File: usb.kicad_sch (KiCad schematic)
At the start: 23 parts, among them IC2 USB Hub, J2 2-Port USB, J3 2-Port USB

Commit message: USB stack changes
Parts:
- added C30, C31: 27pF, Capacitor_SMD:C_0805_2012Metric, symbol group127:0805Capacitor
- added J8: USB_Headers, Connector_PinHeader_2.54mm:PinHeader_1x04_P2.54mm_Vertical, symbol Connector:Conn_01x04_Pin
- added R31: 1.5kOhm, Resistor_SMD:R_0805_2012Metric, symbol group127:Resistor
- added Y1: ECS-060-20-4X-DU, group127:XTAL_ECS-160-20-4X, symbol group127:ECS-060-20-4X-DU
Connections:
- net TSTPLL/48MCLK is gone; now on net GND: IC2.27 (TSTPLL/48MCLK)
- net 3V3: no longer IC2.30 (XTAL1), IC2.31 (TSTMODE)
- net 5V: now also J8.1 (Pin_1)
- net GND: now also IC2.31 (TSTMODE), C30.2, C31.2, J8.4 (Pin_4)
- net at IC2.29 (XTAL2): now also R31.2
- net D0+: no longer names the net of IC2.1 (D0+)
- net D0+: now also J8.2 (Pin_2)
- net D0-: no longer names the net of IC2.2 (D0-)
- net D0-: now also J8.3 (Pin_3)
- new net: C30.1, R31.1, Y1.2
- new net: C31.1, IC2.30 (XTAL1), Y1.1
- no-connect marks 10 -> 9

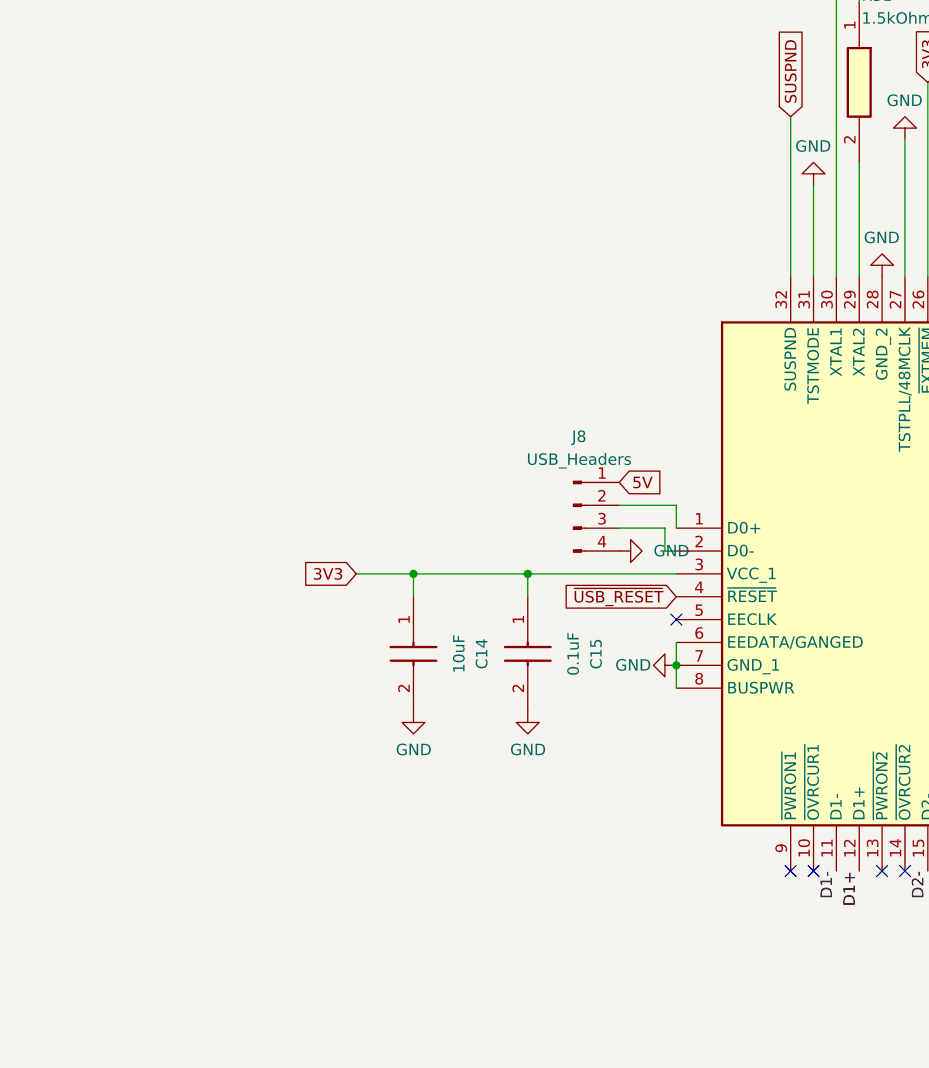
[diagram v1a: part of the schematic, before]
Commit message: USB fixes
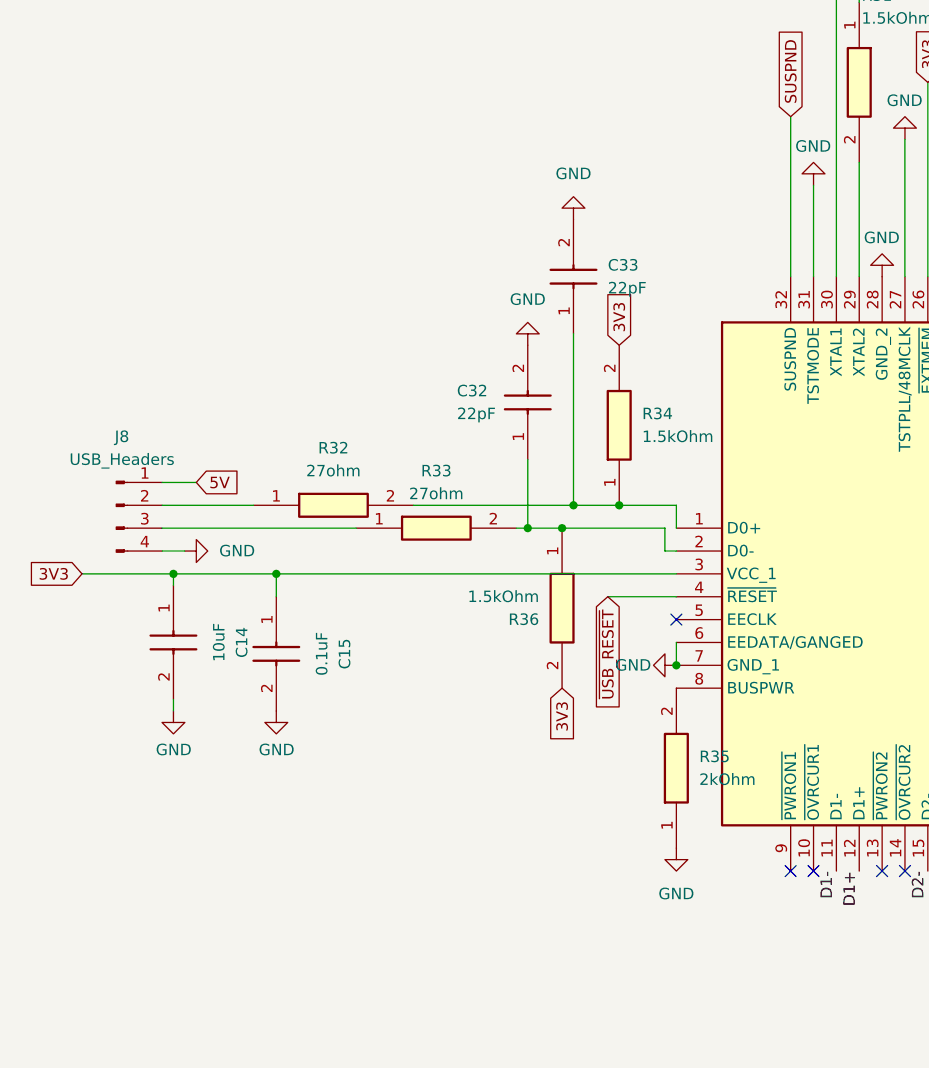
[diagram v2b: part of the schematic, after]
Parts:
- added C32, C33: 22pF, Capacitor_SMD:C_0805_2012Metric, symbol group127:0805Capacitor
- added R32, R33: 27ohm, Resistor_SMD:R_0805_2012Metric, symbol group127:Resistor
- added R34, R36: 1.5kOhm, Resistor_SMD:R_0805_2012Metric, symbol group127:Resistor
- added R35: 2kOhm, Resistor_SMD:R_0805_2012Metric, symbol group127:Resistor
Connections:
- net 3V3: now also R34.2, R36.2
- net GND: now also C32.2, C33.2, R35.1; no longer IC2.8 (BUSPWR)
- net at IC2.1 (D0+): now also C33.1, R32.2, R34.1; no longer J8.2 (Pin_2)
- net at J8.3 (Pin_3): now also R33.1; no longer IC2.2 (D0-)
- new net: J8.2 (Pin_2), R32.1
- new net: C32.1, IC2.2 (D0-), R33.2, R36.1
- new net: IC2.8 (BUSPWR), R35.2
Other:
- moved on the sheet: C14, C15, J8

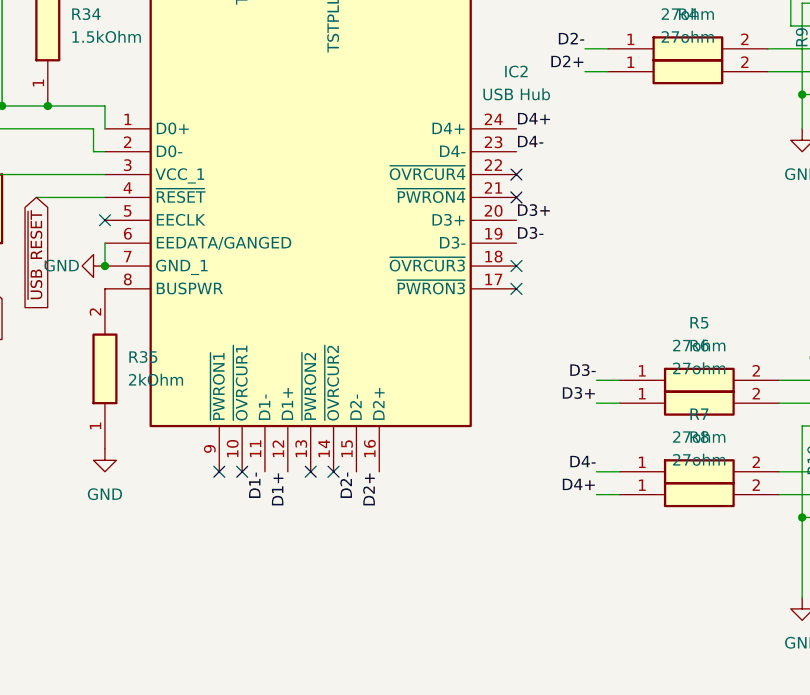
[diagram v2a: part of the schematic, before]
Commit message: overcurrent fixes
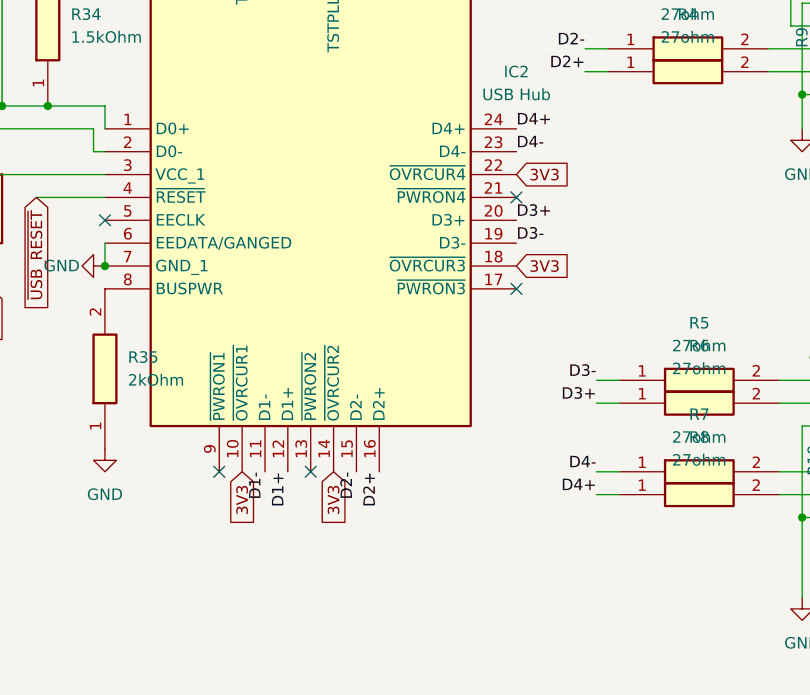
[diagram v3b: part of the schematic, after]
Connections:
- net 3V3: now also IC2.10 (~{OVRCUR1}), IC2.14 (~{OVRCUR2}), IC2.18 (~{OVRCUR3}), IC2.22 (~{OVRCUR4})
- no-connect marks 9 -> 5
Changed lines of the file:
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@@
-	)
-	(no_connect
-		(at 154.94 113.03)
 	)
 	(no_connect
@@
 	)
 	(no_connect
-		(at 134.62 135.89)
-	)
-	(no_connect
-		(at 124.46 135.89)
-	)
-	(no_connect
 		(at 109.22 107.95)
-	)
-	(no_connect
-		(at 154.94 102.87)
 	)
 	(wire
@@
 	(global_label "3V3"
 		(shape input)
+		(at 154.94 102.87 0)
+		(fields_autoplaced yes)
+		(effects
+			(font
+				(size 1.27 1.27)
+			)
+			(justify left)
+		)
+		(property "Intersheetrefs" "${INTERSHEET_REFS}"
+			(at 161.4328 102.87 0)
+			(effects
+				(font
+					(size 1.27 1.27)
+				)
+				(justify left)
+				(hide yes)
+			)
+		)
+	)
+	(global_label "3V3"
+		(shape input)
 		(at 102.87 77.47 90)
 		(fields_autoplaced yes)
@@
 		)
 	)
+	(global_label "3V3"
+		(shape input)
+		(at 124.46 135.89 270)
+		(fields_autoplaced yes)
+		(effects
+			(font
+				(size 1.27 1.27)
+			)
+			(justify right)
+		)
+		(property "Intersheetrefs" "${INTERSHEET_REFS}"
+			(at 124.46 142.3828 90)
+			(effects
+				(font
+					(size 1.27 1.27)
+				)
+				(justify right)
+				(hide yes)
+			)
+		)
+	)
 	(global_label "SUSPND"
 		(shape input)
@@
 				(hide yes)
 			)
+		)
+	)
+	(global_label "3V3"
+		(shape input)
+		(at 134.62 135.89 270)
+		(fields_autoplaced yes)
+		(effects
+			(font
+				(size 1.27 1.27)
+			)
+			(justify right)
+		)
+		(property "Intersheetrefs" "${INTERSHEET_REFS}"
+			(at 134.62 142.3828 90)
+			(effects
+				(font
+					(size 1.27 1.27)
+				)
+				(justify right)
+				(hide yes)
+			)
+		)
+	)
+	(global_label "3V3"
+		(shape input)
+		(at 154.94 113.03 0)
+		(fields_autoplaced yes)
+		(effects
+			(font
+				(size 1.27 1.27)
+			)
+			(justify left)
+		)
+		(property "Intersheetrefs" "${INTERSHEET_REFS}"
+			(at 161.4328 113.03 0)
+			(effects
+				(font
+					(size 1.27 1.27)
+				)
+				(justify left)
+				(hide yes)
+			)
